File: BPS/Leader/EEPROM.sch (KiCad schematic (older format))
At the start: 4 parts, among them U4 M24128

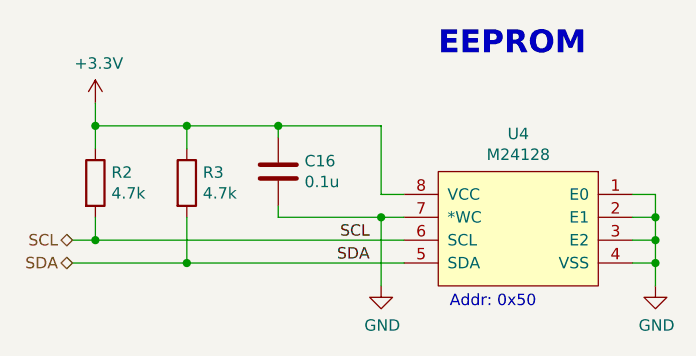
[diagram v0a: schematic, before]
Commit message: Simplifies dc-dc converter schematics
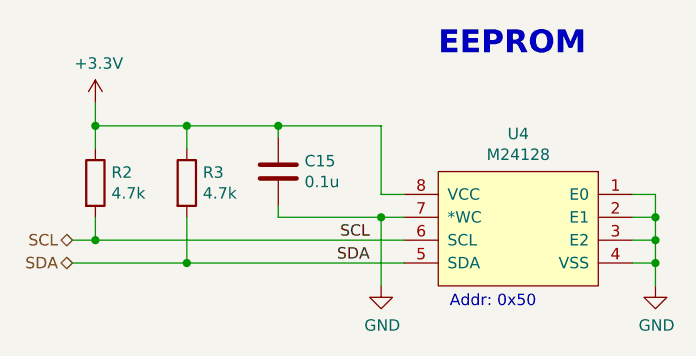
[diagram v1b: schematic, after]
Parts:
- renumbered C16 to C15
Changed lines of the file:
@@
 SCL
 $Comp
-L Device:C C16
+L Device:C C15
 U 1 1 5C35143C
 P 3200 2800
-F 0 "C16" H 3315 2846 50  0000 L CNN
+F 0 "C15" H 3315 2846 50  0000 L CNN
 F 1 "0.1u" H 3315 2755 50  0000 L CNN
 F 2 "Capacitor_SMD:C_0805_2012Metric" H 3238 2650 50  0001 C CNN
